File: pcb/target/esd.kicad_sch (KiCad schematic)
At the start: 0 parts

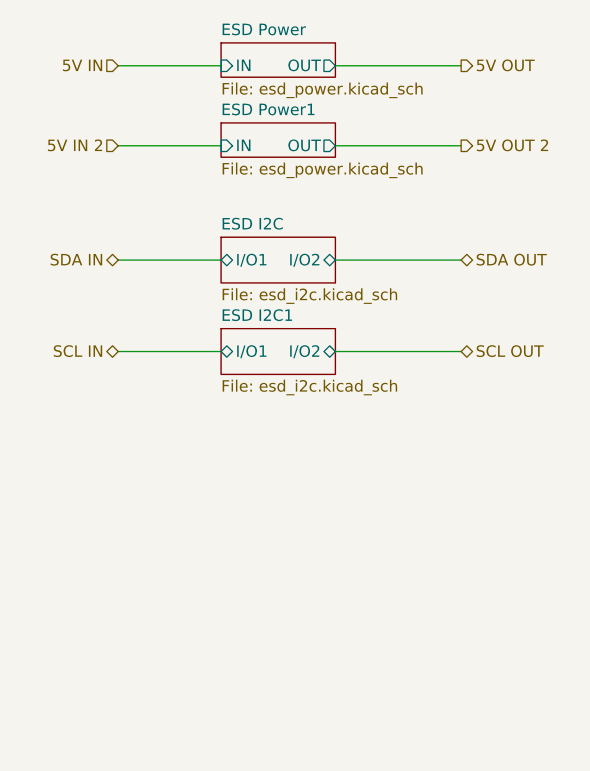
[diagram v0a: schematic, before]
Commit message: Switched to attiny1614 and fixed esd for the i2c lines (target pcb)
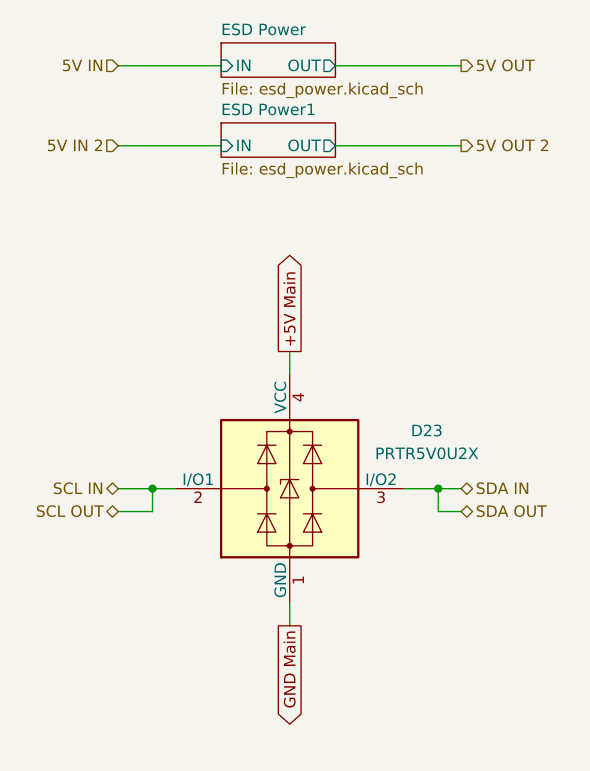
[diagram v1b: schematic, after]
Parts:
- added D23: PRTR5V0U2X, Package_TO_SOT_SMD:SOT-143, symbol Power_Protection:PRTR5V0U2X
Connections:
- net SCL IN: now also D23.2 (I/O1)
- net SDA IN: now also D23.3 (I/O2)
- new net +5V Main: D23.4 (VCC)
- new net GND Main: D23.1 (GND)
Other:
- removed sheet ESD I2C
- removed sheet ESD I2C1
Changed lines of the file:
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@@
 	(generator_version "9.0")
 	(paper "A4")
-	(wire
-		(pts
-			(xy 88.9 124.46) (xy 100.33 124.46)
-		)
-		(stroke
-			(width 0)
-			(type default)
-		)
-	)
-	(wire
-		(pts
-			(xy 113.03 124.46) (xy 127 124.46)
-		)
-		(stroke
-			(width 0)
-			(type default)
-		)
-	)
-	(wire
-		(pts
-			(xy 88.9 114.3) (xy 100.33 114.3)
+	(junction
+		(at 124.46 139.7)
+		(diameter 0)
+		(color 0 0 0 0)
+	)
+	(junction
+		(at 92.71 139.7)
+		(diameter 0)
+		(color 0 0 0 0)
+	)
+	(wire
+		(pts
+			(xy 120.65 139.7) (xy 124.46 139.7)
+		)
+		(stroke
+			(width 0)
+			(type default)
+		)
+	)
+	(wire
+		(pts
+			(xy 107.95 124.46) (xy 107.95 127)
+		)
+		(stroke
+			(width 0)
+			(type default)
+		)
+	)
+	(wire
+		(pts
+			(xy 124.46 139.7) (xy 127 139.7)
+		)
+		(stroke
+			(width 0)
+			(type default)
+		)
+	)
+	(wire
+		(pts
+			(xy 124.46 142.24) (xy 124.46 139.7)
 		)
 		(stroke
@@
 	(wire
 		(pts
+			(xy 92.71 139.7) (xy 95.25 139.7)
+		)
+		(stroke
+			(width 0)
+			(type default)
+		)
+	)
+	(wire
+		(pts
+			(xy 88.9 139.7) (xy 92.71 139.7)
+		)
+		(stroke
+			(width 0)
+			(type default)
+		)
+	)
+	(wire
+		(pts
 			(xy 88.9 92.71) (xy 100.33 92.71)
 		)
@@
 	(wire
 		(pts
-			(xy 113.03 114.3) (xy 127 114.3)
+			(xy 88.9 142.24) (xy 92.71 142.24)
+		)
+		(stroke
+			(width 0)
+			(type default)
+		)
+	)
+	(wire
+		(pts
+			(xy 92.71 142.24) (xy 92.71 139.7)
 		)
 		(stroke
@@
 			(width 0)
 			(type default)
+		)
+	)
+	(wire
+		(pts
+			(xy 107.95 152.4) (xy 107.95 154.94)
+		)
+		(stroke
+			(width 0)
+			(type default)
+		)
+	)
+	(wire
+		(pts
+			(xy 127 142.24) (xy 124.46 142.24)
+		)
+		(stroke
+			(width 0)
+			(type default)
+		)
+	)
+	(global_label "+5V Main"
+		(shape output)
+		(at 107.95 124.46 90)
+		(fields_autoplaced yes)
+		(effects
+			(font
+				(size 1.27 1.27)
+			)
+			(justify left)
+		)
+		(property "Intersheetrefs" "${INTERSHEET_REFS}"
+			(at 107.95 112.2825 90)
+			(effects
+				(font
+					(size 1.27 1.27)
+				)
+				(justify left)
+				(hide yes)
+			)
+		)
+	)
+	(global_label "GND Main"
+		(shape output)
+		(at 107.95 154.94 270)
+		(fields_autoplaced yes)
+		(effects
+			(font
+				(size 1.27 1.27)
+			)
+			(justify right)
+		)
+		(property "Intersheetrefs" "${INTERSHEET_REFS}"
+			(at 107.95 167.1175 90)
+			(effects
+				(font
+					(size 1.27 1.27)
+				)
+				(justify right)
+				(hide yes)
+			)
 		)
 	)
@@
 	(hierarchical_label "SDA OUT"
 		(shape bidirectional)
-		(at 127 114.3 0)
+		(at 127 142.24 0)
 		(effects
 			(font
@@
 	(hierarchical_label "SCL OUT"
 		(shape bidirectional)
-		(at 127 124.46 0)
-		(effects
-			(font
-				(size 1.27 1.27)
-			)
-			(justify left)
+		(at 88.9 142.24 180)
+		(effects
+			(font
+				(size 1.27 1.27)
+			)
+			(justify right)
 		)
 	)
 	(hierarchical_label "SDA IN"
 		(shape bidirectional)
-		(at 88.9 114.3 180)
-		(effects
-			(font
-				(size 1.27 1.27)
-			)
-			(justify right)
+		(at 127 139.7 0)
+		(effects
+			(font
+				(size 1.27 1.27)
+			)
+			(justify left)
 		)
 	)
@@
 	(hierarchical_label "SCL IN"
 		(shape bidirectional)
-		(at 88.9 124.46 180)
+		(at 88.9 139.7 180)
 		(effects
 			(font
@@
 			)
 			(justify right)
+		)
+	)
+	(symbol
+		(lib_id "Power_Protection:PRTR5V0U2X")
+		(at 107.95 139.7 0)
+		(unit 1)
+		(exclude_from_sim no)
+		(in_bom yes)
+		(on_board yes)
+		(dnp no)
+		(fields_autoplaced yes)
+		(property "Reference" "D23"
+			(at 123.19 133.2798 0)
+			(effects
+				(font
+					(size 1.27 1.27)
+				)
+			)
+		)
+		(property "Value" "PRTR5V0U2X"
+			(at 123.19 135.8198 0)
+			(effects
+				(font
+					(size 1.27 1.27)
+				)
+			)
+		)
+		(property "Footprint" "Package_TO_SOT_SMD:SOT-143"
+			(at 109.474 139.7 0)
+			(effects
+				(font
+					(size 1.27 1.27)
+				)
+				(hide yes)
+			)
+		)
+		(property "Datasheet" "https://assets.nexperia.com/documents/data-sheet/PRTR5V0U2X.pdf"
+			(at 109.474 139.7 0)
+			(effects
+				(font
+					(size 1.27 1.27)
+				)
+				(hide yes)
+			)
+		)
+		(property "Description" "Ultra low capacitance double rail-to-rail ESD protection diode, SOT-143"
+			(at 107.95 139.7 0)
+			(effects
+				(font
+					(size 1.27 1.27)
+				)
+				(hide yes)
+			)
+		)
+		(property "LCSC" "C5180302"
+			(at 107.95 139.7 0)
+			(effects
+				(font
+					(size 1.27 1.27)
+				)
+				(hide yes)
+			)
+		)
+		(pin "4"
+		)
+		(pin "2"
+		)
+		(pin "1"
+		)
+		(pin "3"
+		)
+		(instances
+			(project "target"
+				(path "/1c02f793-f381-44cb-838a-dbb787484d0c/b3335a6a-71bd-476c-b233-926fd1552a47"
+					(reference "D23")
+					(unit 1)
+				)
+			)
 		)
 	)
@@
 				)
 			)
-		)
-	)
-	(sheet
-		(at 100.33 111.76)
-		(size 12.7 5.08)
-		(exclude_from_sim no)
-		(in_bom yes)
-		(on_board yes)
-		(dnp no)
-		(fields_autoplaced yes)
-		(stroke
-			(width 0.1524)
-			(type solid)
-		)
-		(fill
-			(color 0 0 0 0.0000)
-		)
-		(property "Sheetname" "ESD I2C"
-			(at 100.33 111.0484 0)
-			(effects
-				(font
-					(size 1.27 1.27)
-				)
-				(justify left bottom)
-			)
-		)
-		(property "Sheetfile" "esd_i2c.kicad_sch"
-			(at 100.33 117.4246 0)
-			(effects
-				(font
-					(size 1.27 1.27)
-				)
-				(justify left top)
-			)
-		)
-		(pin "I{slash}O1" bidirectional
-			(at 100.33 114.3 180)
-			(effects
-				(font
-					(size 1.27 1.27)
-				)
-				(justify left)
-			)
-		)
-		(pin "I{slash}O2" bidirectional
-			(at 113.03 114.3 0)
-			(effects
-				(font
-					(size 1.27 1.27)
-				)
-				(justify right)
-			)
-		)
-		(instances
-			(project "target"
-				(path "/1c02f793-f381-44cb-838a-dbb787484d0c/b3335a6a-71bd-476c-b233-926fd1552a47"
-					(page "15")
-				)
-			)
-		)
-	)
-	(sheet
-		(at 100.33 121.92)
-		(size 12.7 5.08)
-		(exclude_from_sim no)
-		(in_bom yes)
-		(on_board yes)
-		(dnp no)
-		(fields_autoplaced yes)
-		(stroke
-			(width 0.1524)
-			(type solid)
-		)
-		(fill
-			(color 0 0 0 0.0000)
-		)
-		(property "Sheetname" "ESD I2C1"
-			(at 100.33 121.2084 0)
-			(effects
-				(font
-					(size 1.27 1.27)
-				)
-				(justify left bottom)
-			)
-		)
-		(property "Sheetfile" "esd_i2c.kicad_sch"
-			(at 100.33 127.5846 0)
-			(effects
-				(font
-					(size 1.27 1.27)
-				)
-				(justify left top)
-			)
-		)
-		(pin "I{slash}O1" bidirectional
-			(at 100.33 124.46 180)
-			(effects
-				(font
-					(size 1.27 1.27)
-				)
-				(justify left)
-			)
-		)
-		(pin "I{slash}O2" bidirectional
-			(at 113.03 124.46 0)
-			(effects
-				(font
-					(size 1.27 1.27)
-				)
-				(justify right)
-			)
-		)
-		(instances
-			(project "target"
-				(path "/1c02f793-f381-44cb-838a-dbb787484d0c/b3335a6a-71bd-476c-b233-926fd1552a47"
-					(page "13")
-				)
-			)
